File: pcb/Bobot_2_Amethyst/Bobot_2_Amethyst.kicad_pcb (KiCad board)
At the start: 2 copper layers, 123.5 x 60 mm, 14 parts, among them U1 ESP32_DevKit_V1_DOIT

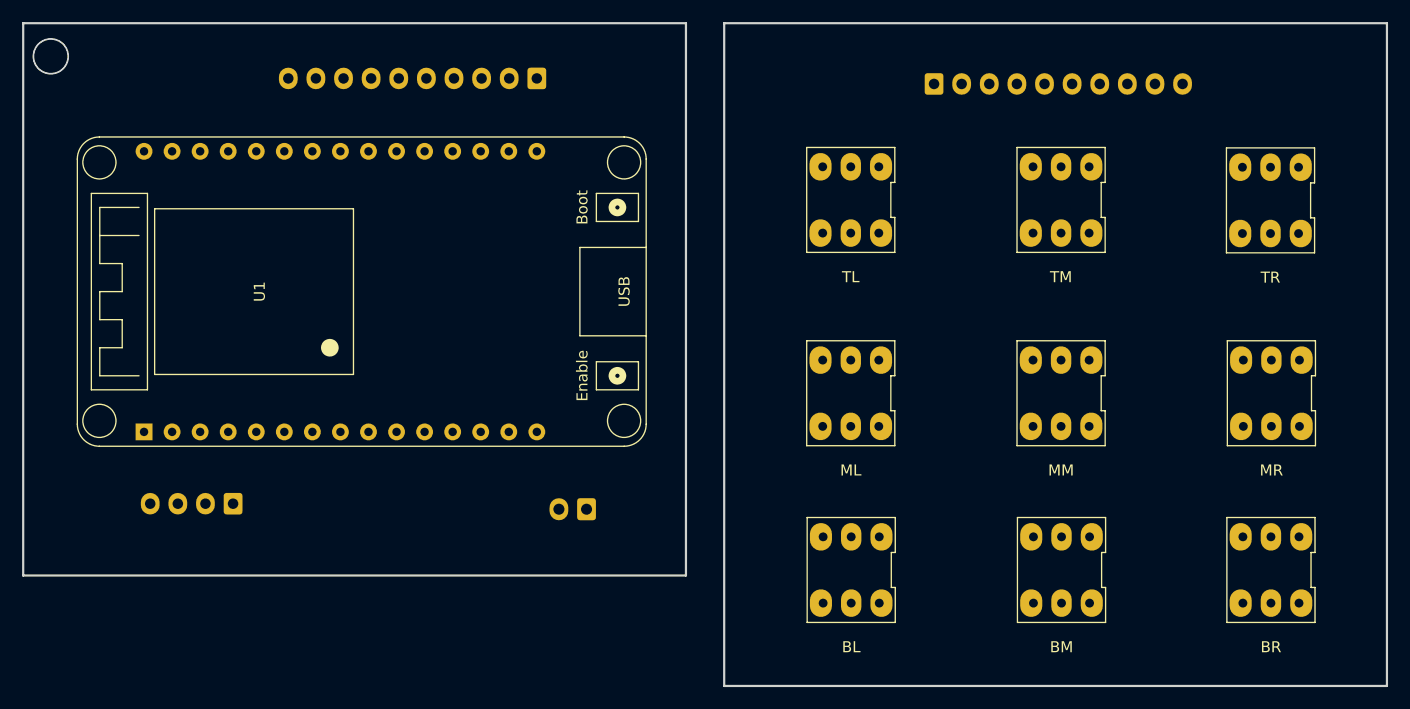
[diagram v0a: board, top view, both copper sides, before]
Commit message: pcb: update buttons alignment
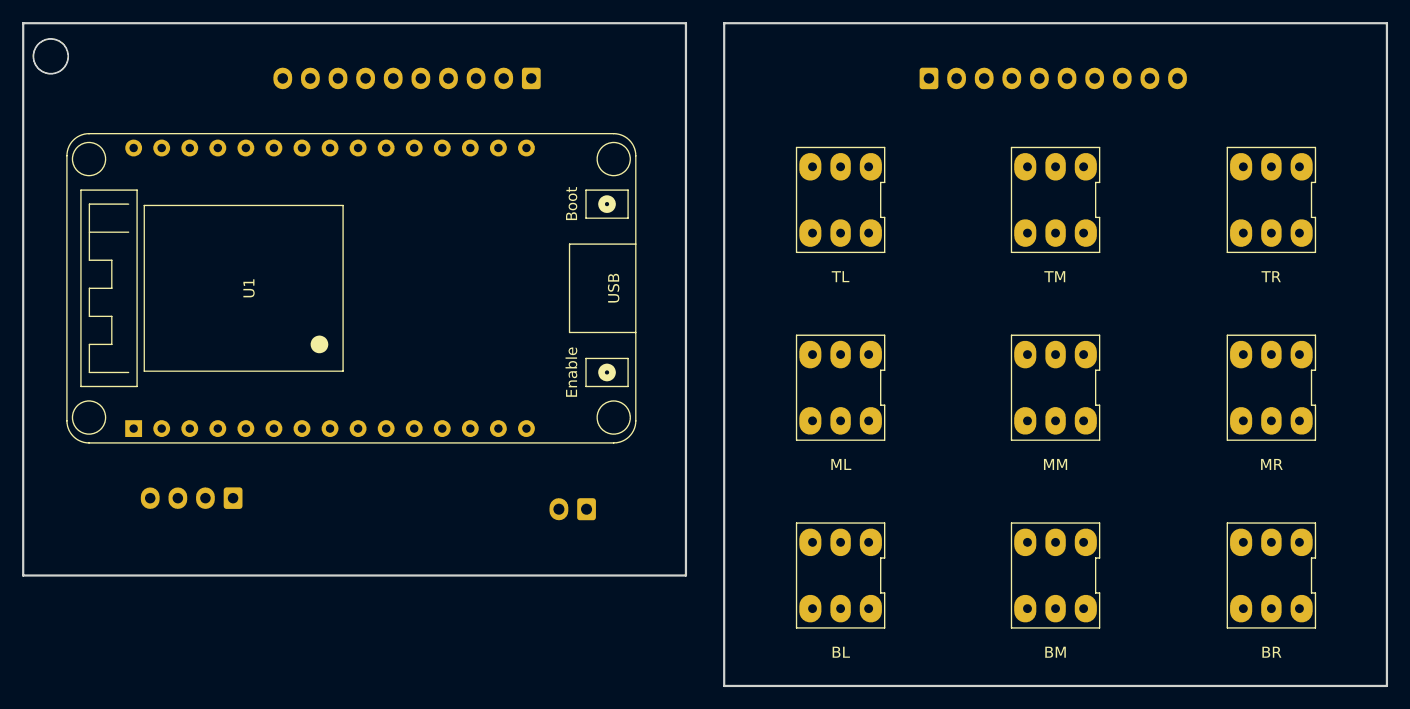
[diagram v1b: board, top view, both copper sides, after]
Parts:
- moved BtnBL1 1.08 mm to (86.0, 62.0)
- moved BtnML1 1.05 mm to (86.0, 45.0)
- moved U1 0.99 mm to (22.0, 36.0)
- moved BtnTL1 0.92 mm to (86.0, 28.0)
- moved BtnBM1 0.74 mm to (105.5, 62.0)
- moved BtnMM1 0.71 mm to (105.5, 45.0)
- moved BtnBusOut1 0.68 mm to (94.0, 17.0)
- moved BtnBR1 0.50 mm to (125.0, 62.0)
- moved BtnBusIn1 0.50 mm to (58.0, 17.0)
- moved BtnMR1 0.50 mm to (125.0, 45.0)
- moved BtnTM1 0.50 mm to (105.5, 28.0)
- moved Display_connector1 0.50 mm to (31.0, 55.0)
- moved BtnTR1 0.09 mm to (125.0, 28.0)
